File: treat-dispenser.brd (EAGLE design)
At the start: 31.8 x 47 mm, 36 parts, among them U1 MCP73831, U3 ATMEGA32U4, Y1 16MHz

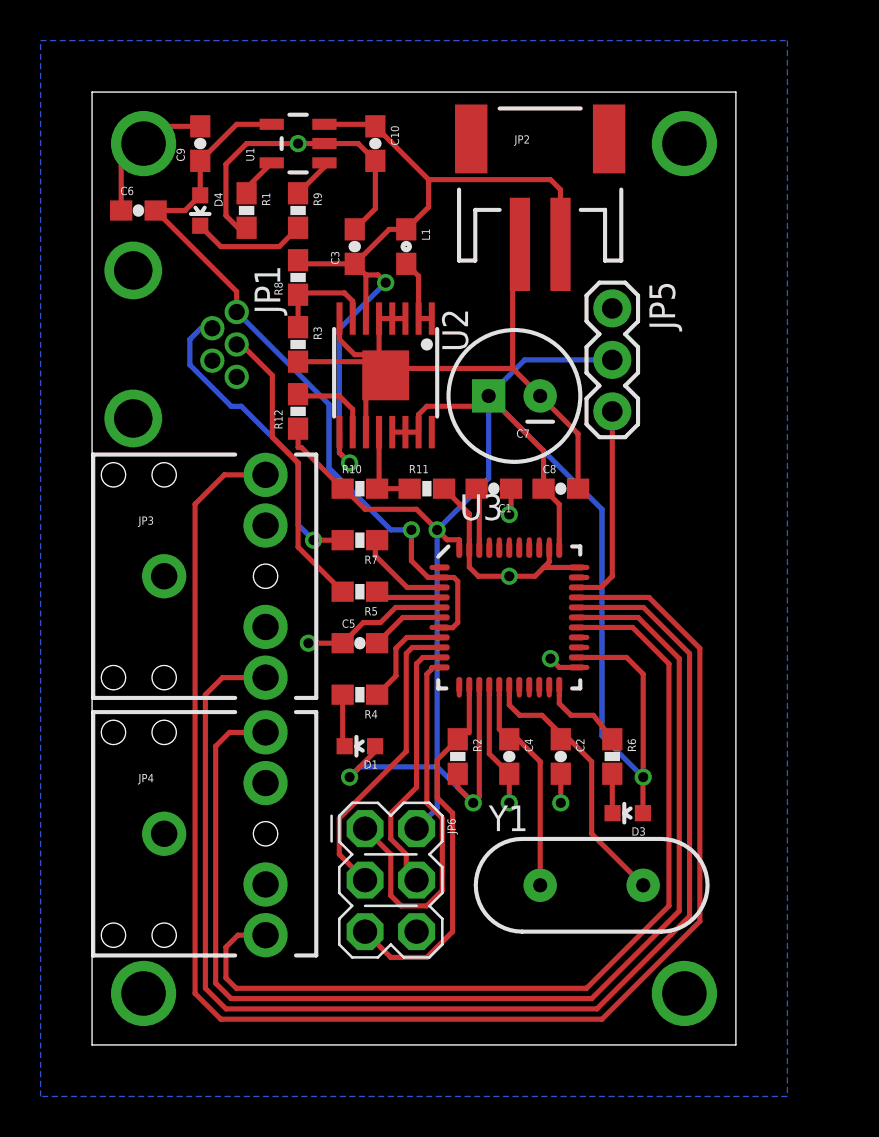
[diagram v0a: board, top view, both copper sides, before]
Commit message: fixed some routing issues, added part numbers
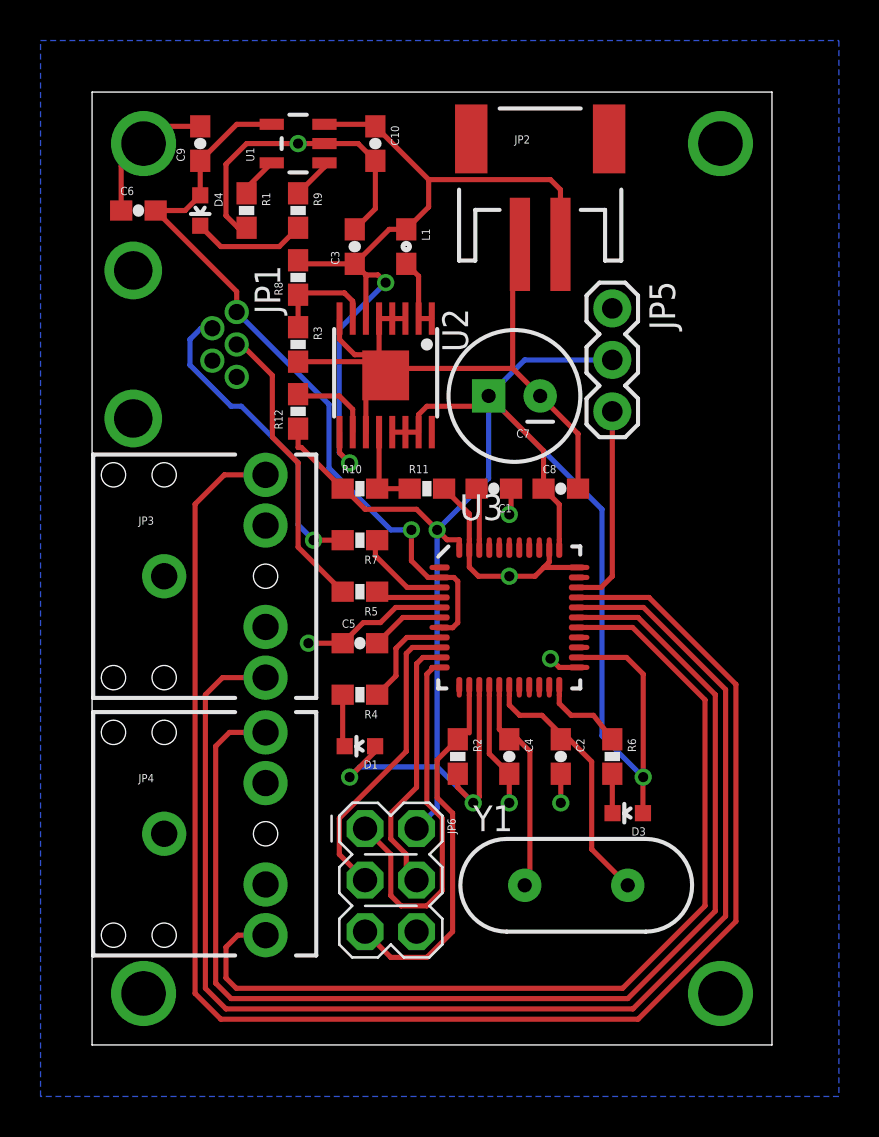
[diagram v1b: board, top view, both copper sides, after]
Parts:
- added FRAME1: FRAME-LETTER, SparkFun-Aesthetics:CREATIVE_COMMONS
- JP1: value USB-MB-H -> WM17115-ND
- U2: value (none) -> TPS61032
- moved Y1 0.76 mm to (23.9, 7.87)
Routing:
- net D9: track 62.9 -> 65.5 mm
- net D8: track 57.7 -> 60.2 mm
- net D10: track 75.7 -> 78.2 mm
- net D6: track 44.2 -> 46.7 mm
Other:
- board size 31.8 x 47 mm -> 33.5 x 47 mm
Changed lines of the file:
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@@
 <layer number="19" name="Unrouted" color="6" fill="1" visible="yes" active="yes"/>
 <layer number="20" name="Dimension" color="15" fill="1" visible="yes" active="yes"/>
-<layer number="21" name="tPlace" color="7" fill="1" visible="yes" active="yes"/>
-<layer number="22" name="bPlace" color="7" fill="1" visible="yes" active="yes"/>
+<layer number="21" name="tPlace" color="14" fill="1" visible="yes" active="yes"/>
+<layer number="22" name="bPlace" color="14" fill="1" visible="yes" active="yes"/>
 <layer number="23" name="tOrigins" color="15" fill="1" visible="yes" active="yes"/>
 <layer number="24" name="bOrigins" color="15" fill="1" visible="yes" active="yes"/>
@@
 <board>
 <plain>
-<wire x1="0" y1="0" x2="31.75" y2="0" width="0" layer="20"/>
-<wire x1="31.75" y1="0" x2="31.75" y2="46.99" width="0" layer="20"/>
-<wire x1="31.75" y1="46.99" x2="0" y2="46.99" width="0" layer="20"/>
+<wire x1="0" y1="0" x2="33.528" y2="0" width="0" layer="20"/>
+<wire x1="33.528" y1="0" x2="33.528" y2="46.99" width="0" layer="20"/>
+<wire x1="33.528" y1="46.99" x2="0" y2="46.99" width="0" layer="20"/>
 <wire x1="0" y1="46.99" x2="0" y2="0" width="0" layer="20"/>
 </plain>
@@
 <element name="D3" library="SparkFun" package="LED-0603" value="Green" x="26.416" y="11.43" rot="R90"/>
 <element name="U3" library="Testing" package="QFN-44-NOPAD_1:1-OUTFAKES" value="ATMEGA32U4" x="20.574" y="21.082"/>
-<element name="Y1" library="SparkFun" package="HC49US" value="16MHz" x="24.638" y="7.874"/>
+<element name="Y1" library="SparkFun" package="HC49US" value="16MHz" x="23.876" y="7.874"/>
 <element name="C2" library="SparkFun" package="0603-CAP" value="22pF" x="23.114" y="14.224" rot="R270"/>
 <element name="C4" library="SparkFun" package="0603-CAP" value="22pF" x="20.574" y="14.224" rot="R270"/>
@@
 <element name="R5" library="SparkFun" package="0603-RES" value="22" x="13.208" y="22.352" rot="R180"/>
 <element name="R7" library="SparkFun" package="0603-RES" value="22" x="13.208" y="24.892" rot="R180"/>
-<element name="JP1" library="SparkFun-Connectors" package="USB-MB-H" value="USB-MB-H" x="2.032" y="34.544"/>
+<element name="JP1" library="SparkFun-Connectors" package="USB-MB-H" value="WM17115-ND" x="2.032" y="34.544"/>
 <element name="C9" library="SparkFun" package="0603-CAP" value="4.7uF" x="5.334" y="44.45" rot="R90"/>
 <element name="C10" library="SparkFun" package="0603-CAP" value="4.7uF" x="13.97" y="44.45" rot="R270"/>
@@
 <element name="R1" library="SparkFun" package="0603-RES" value="10K" x="7.62" y="41.148" rot="R270"/>
 <element name="JP2" library="SparkFun" package="JST-2-SMD" value="LiPo" x="22.098" y="43.18"/>
-<element name="U2" library="tps6103x" package="TSSOP-16" value="" x="14.478" y="33.02" rot="R180"/>
+<element name="U2" library="tps6103x" package="TSSOP-16" value="TPS61032" x="14.478" y="33.02" rot="R180"/>
 <element name="R3" library="SparkFun" package="0603-RES" value="300K" x="10.16" y="34.544" rot="R270"/>
 <element name="R8" library="SparkFun" package="0603-RES" value="1.62M" x="10.16" y="37.846" rot="R90"/>
@@
 <element name="C7" library="SparkFun-Capacitors" package="CPOL-RADIAL-100UF-25V" value="220uF" x="20.828" y="32.004" rot="R180"/>
 <element name="C8" library="SparkFun" package="0603-CAP" value="10uF" x="23.114" y="27.432"/>
+<element name="FRAME1" library="SparkFun-Aesthetics" package="CREATIVE_COMMONS" value="FRAME-LETTER" x="19.05" y="49.53"/>
 </elements>
 <signals>
@@
 <contactref element="U2" pad="PAD"/>
 <via x="2.54" y="44.45" extent="1-16" drill="2.2"/>
-<via x="29.21" y="44.45" extent="1-16" drill="2.2"/>
+<via x="30.988" y="44.45" extent="1-16" drill="2.2"/>
 <via x="2.54" y="2.54" extent="1-16" drill="2.2"/>
-<via x="29.21" y="2.54" extent="1-16" drill="2.2"/>
+<via x="30.988" y="2.54" extent="1-16" drill="2.2"/>
 <polygon width="0.254" layer="16">
 <vertex x="-2.54" y="49.53"/>
-<vertex x="34.29" y="49.53"/>
-<vertex x="34.29" y="-2.54"/>
+<vertex x="36.83" y="49.53"/>
+<vertex x="36.83" y="-2.54"/>
 <vertex x="-2.54" y="-2.54"/>
 </polygon>
@@
 <wire x1="5.588" y1="17.272" x2="5.588" y2="2.794" width="0.254" layer="1"/>
 <wire x1="5.588" y1="2.794" x2="6.604" y2="1.778" width="0.254" layer="1"/>
-<wire x1="6.604" y1="1.778" x2="24.892" y2="1.778" width="0.254" layer="1"/>
-<wire x1="24.892" y1="1.778" x2="29.464" y2="6.35" width="0.254" layer="1"/>
-<wire x1="29.464" y1="6.35" x2="29.464" y2="19.304" width="0.254" layer="1"/>
+<wire x1="6.604" y1="1.778" x2="26.67" y2="1.778" width="0.254" layer="1"/>
+<wire x1="26.67" y1="1.778" x2="31.242" y2="6.35" width="0.254" layer="1"/>
+<wire x1="31.242" y1="6.35" x2="31.242" y2="17.526" width="0.254" layer="1"/>
 <wire x1="24.4035" y1="21.575" x2="27.193" y2="21.575" width="0.254" layer="1"/>
-<wire x1="27.193" y1="21.575" x2="29.464" y2="19.304" width="0.254" layer="1"/>
+<wire x1="27.193" y1="21.575" x2="31.242" y2="17.526" width="0.254" layer="1"/>
 </signal>
 <signal name="D8">
@@
 <contactref element="JP4" pad="RING"/>
 <wire x1="23.9105" y1="21.082" x2="26.924" y2="21.082" width="0.254" layer="1"/>
-<wire x1="26.924" y1="21.082" x2="28.956" y2="19.05" width="0.254" layer="1"/>
-<wire x1="28.956" y1="19.05" x2="28.956" y2="6.604" width="0.254" layer="1"/>
-<wire x1="28.956" y1="6.604" x2="24.638" y2="2.286" width="0.254" layer="1"/>
-<wire x1="24.638" y1="2.286" x2="6.858" y2="2.286" width="0.254" layer="1"/>
+<wire x1="26.924" y1="21.082" x2="30.734" y2="17.272" width="0.254" layer="1"/>
+<wire x1="30.734" y1="17.272" x2="30.734" y2="6.604" width="0.254" layer="1"/>
+<wire x1="30.734" y1="6.604" x2="26.416" y2="2.286" width="0.254" layer="1"/>
+<wire x1="26.416" y1="2.286" x2="6.858" y2="2.286" width="0.254" layer="1"/>
 <wire x1="6.858" y1="2.286" x2="6.096" y2="3.048" width="0.254" layer="1"/>
 <wire x1="8.556" y1="15.414" x2="6.778" y2="15.414" width="0.254" layer="1"/>
@@
 <wire x1="6.604" y1="4.826" x2="6.604" y2="3.302" width="0.254" layer="1"/>
 <wire x1="6.604" y1="3.302" x2="7.112" y2="2.794" width="0.254" layer="1"/>
-<wire x1="7.112" y1="2.794" x2="24.384" y2="2.794" width="0.254" layer="1"/>
-<wire x1="24.384" y1="2.794" x2="28.448" y2="6.858" width="0.254" layer="1"/>
+<wire x1="7.112" y1="2.794" x2="26.162" y2="2.794" width="0.254" layer="1"/>
+<wire x1="26.162" y1="2.794" x2="30.226" y2="6.858" width="0.254" layer="1"/>
 <wire x1="24.4035" y1="20.589" x2="26.655" y2="20.589" width="0.254" layer="1"/>
-<wire x1="26.655" y1="20.589" x2="28.448" y2="18.796" width="0.254" layer="1"/>
-<wire x1="28.448" y1="18.796" x2="28.448" y2="6.858" width="0.254" layer="1"/>
+<wire x1="26.655" y1="20.589" x2="30.226" y2="17.018" width="0.254" layer="1"/>
+<wire x1="30.226" y1="17.018" x2="30.226" y2="6.858" width="0.254" layer="1"/>
 </signal>
 <signal name="D7">
@@
 <wire x1="5.08" y1="26.67" x2="5.08" y2="2.54" width="0.254" layer="1"/>
 <wire x1="5.08" y1="2.54" x2="6.35" y2="1.27" width="0.254" layer="1"/>
-<wire x1="6.35" y1="1.27" x2="25.146" y2="1.27" width="0.254" layer="1"/>
-<wire x1="25.146" y1="1.27" x2="29.972" y2="6.096" width="0.254" layer="1"/>
+<wire x1="6.35" y1="1.27" x2="26.924" y2="1.27" width="0.254" layer="1"/>
+<wire x1="26.924" y1="1.27" x2="31.75" y2="6.096" width="0.254" layer="1"/>
 <wire x1="24.4035" y1="22.068" x2="27.462" y2="22.068" width="0.254" layer="1"/>
-<wire x1="27.462" y1="22.068" x2="29.972" y2="19.558" width="0.254" layer="1"/>
-<wire x1="29.972" y1="19.558" x2="29.972" y2="6.096" width="0.254" layer="1"/>
+<wire x1="27.462" y1="22.068" x2="31.75" y2="17.78" width="0.254" layer="1"/>
+<wire x1="31.75" y1="17.78" x2="31.75" y2="6.096" width="0.254" layer="1"/>
 </signal>
 <signal name="N$1">
@@
 <contactref element="C4" pad="1"/>
 <wire x1="20.081" y1="17.2525" x2="20.081" y2="15.567" width="0.254" layer="1"/>
-<wire x1="22.098" y1="13.97" x2="22.098" y2="7.874" width="0.254" layer="1"/>
 <wire x1="20.081" y1="15.567" x2="20.574" y2="15.074" width="0.254" layer="1"/>
 <wire x1="20.574" y1="15.074" x2="20.994" y2="15.074" width="0.254" layer="1"/>
-<wire x1="20.994" y1="15.074" x2="22.098" y2="13.97" width="0.254" layer="1"/>
+<wire x1="20.994" y1="15.074" x2="21.59" y2="14.478" width="0.254" layer="1"/>
+<wire x1="21.59" y1="14.478" x2="21.59" y2="8.128" width="0.254" layer="1"/>
+<wire x1="21.59" y1="8.128" x2="21.336" y2="7.874" width="0.254" layer="1"/>
 </signal>
 <signal name="N$2">
@@
 <wire x1="20.574" y1="16.764" x2="21.082" y2="16.256" width="0.254" layer="1"/>
 <wire x1="21.082" y1="16.256" x2="22.186" y2="16.256" width="0.254" layer="1"/>
-<wire x1="24.638" y1="13.97" x2="24.638" y2="10.414" width="0.254" layer="1"/>
-<wire x1="24.638" y1="10.414" x2="27.178" y2="7.874" width="0.254" layer="1"/>
+<wire x1="24.638" y1="13.97" x2="24.638" y2="9.652" width="0.254" layer="1"/>
 <wire x1="23.114" y1="15.074" x2="23.114" y2="15.328" width="0.254" layer="1"/>
 <wire x1="23.114" y1="15.328" x2="22.186" y2="16.256" width="0.254" layer="1"/>
 <wire x1="23.114" y1="15.074" x2="23.534" y2="15.074" width="0.254" layer="1"/>
 <wire x1="23.534" y1="15.074" x2="24.638" y2="13.97" width="0.254" layer="1"/>
+<wire x1="24.638" y1="9.652" x2="26.416" y2="7.874" width="0.254" layer="1"/>
 </signal>
 <signal name="RXI">

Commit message: minor fixes and part changes, added status led
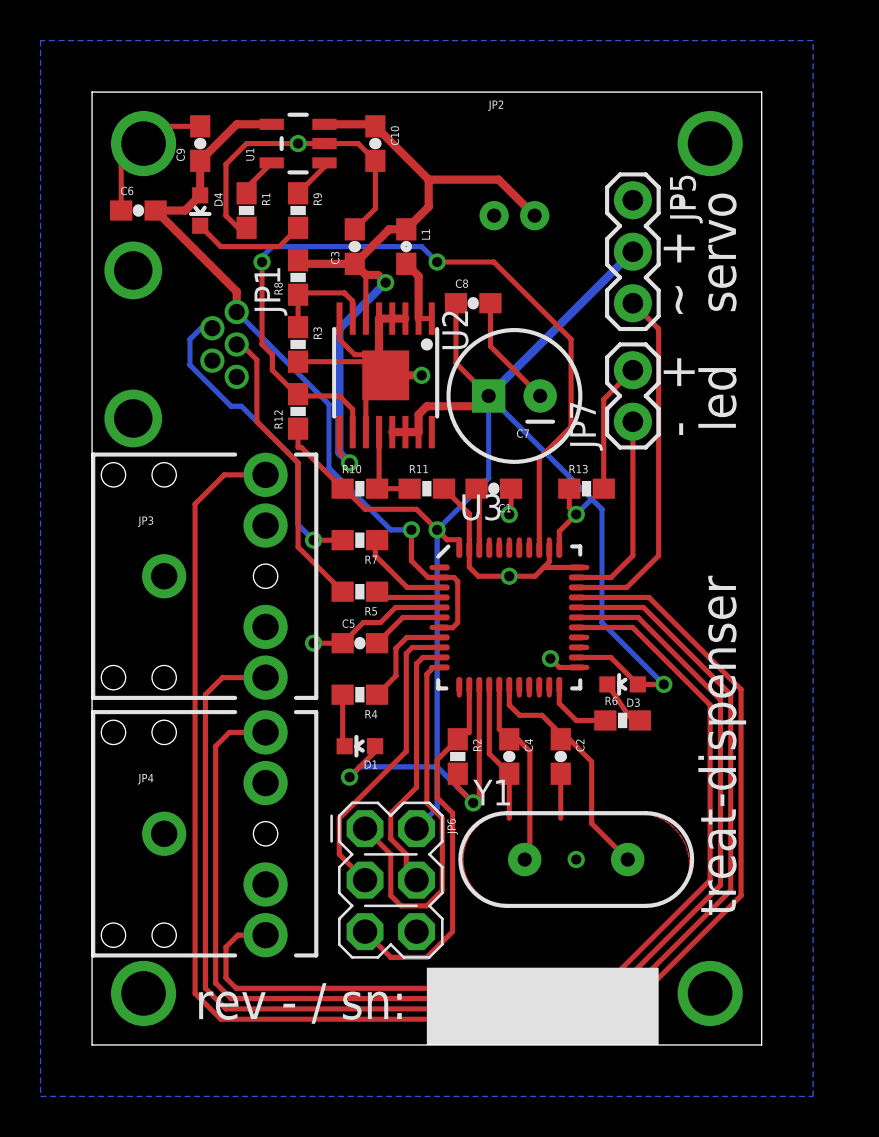
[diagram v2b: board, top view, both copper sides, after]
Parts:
- added JP7: (no value), SparkFun-Connectors:1X02
- added R13: 470, SparkFun:0603-RES
- JP2: value LiPo -> (none); device SparkFun:JST-2-SMD -> SparkFun-Connectors:JST-2-PTH-KIT
- JP3, JP4: value (none) -> SJ1-3523N
- moved C8 10.1 mm to (18.8, 36.6)
- moved D3 6.36 mm to (26.2, 17.8)
- moved JP5 5.43 mm to (26.7, 41.7)
- moved JP2 2.62 mm to (20.8, 40.9)
- moved R6 1.85 mm to (26.2, 16.0), turned to 0 degrees
- moved Y1 1.27 mm to (23.9, 9.14)
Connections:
- removed net ASD: R12.2, U2.10
- new net N$8: JP7.2, R13.2
- net A0: now also R12.2, U2.10
- net D13: now also JP7.1
- net VCC: now also R13.1
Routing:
- net A0: track 0.00 -> 39.6 mm, vias 0 -> 2
- net GND: track 86.2 -> 74.7 mm
- net D13: track 0.00 -> 9.32 mm
- net D5: track 9.61 -> 17.2 mm
- net N$8: track 0.00 -> 6.44 mm
- net VCC: track 103.1 -> 97.9 mm, vias 4 -> 5
- net ASD: track 4.13 -> 0.00 mm
- net V_BATT: track 40.6 -> 37.2 mm
- net N$2: track 12.7 -> 11.4 mm
- net N$1: track 10.4 -> 9.08 mm
- net D8: track 60.2 -> 59.4 mm
- net TXLED: track 3.84 -> 3.03 mm
- net N$7: track 1.95 -> 2.48 mm
- added copper zone on layer 1, net GND
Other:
- board size 33.5 x 47 mm -> 33 x 47 mm
- board text added: "+"
- board text added: "-"
- board text added: "led"
- board text added: "rev - / sn:"
- board text added: "servo"
- board text added: "treat-dispenser"
- board text added: "~"

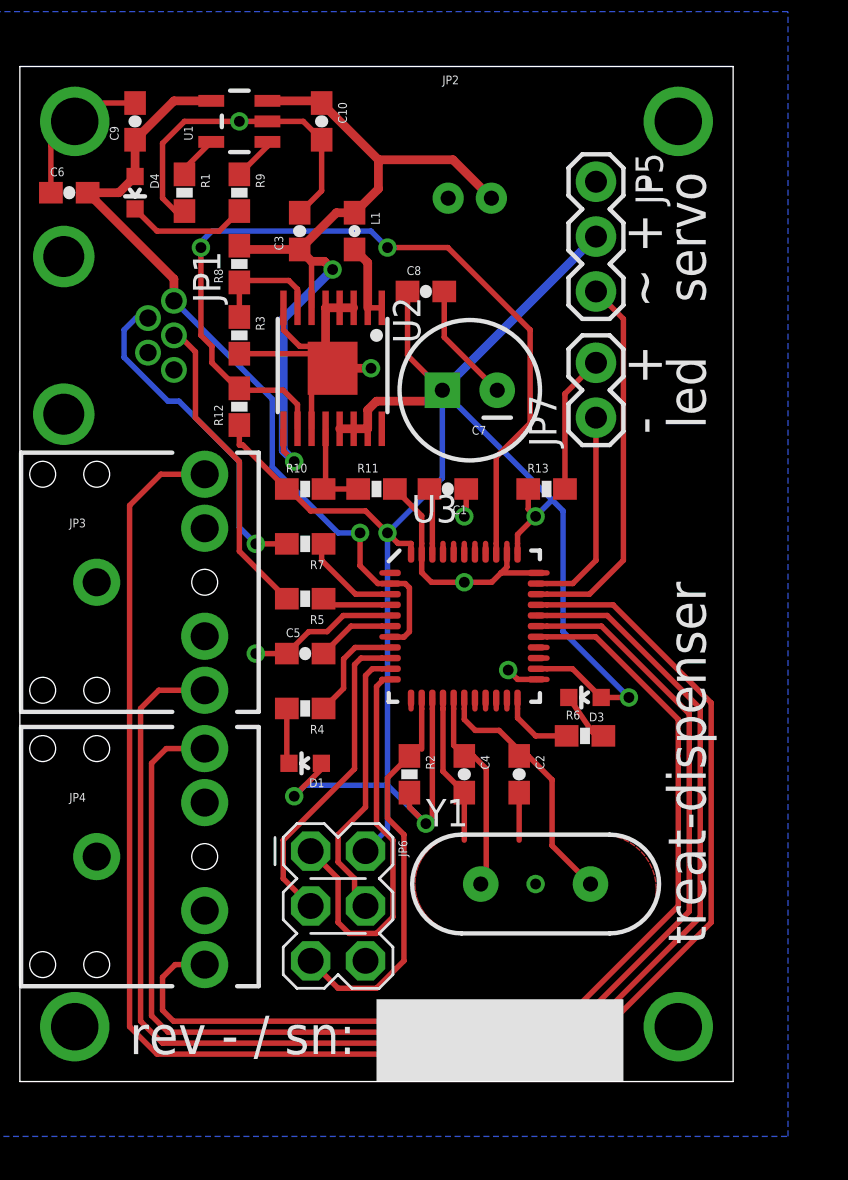
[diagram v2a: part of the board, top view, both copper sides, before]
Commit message: added optional sensor, cleaned up for mfg
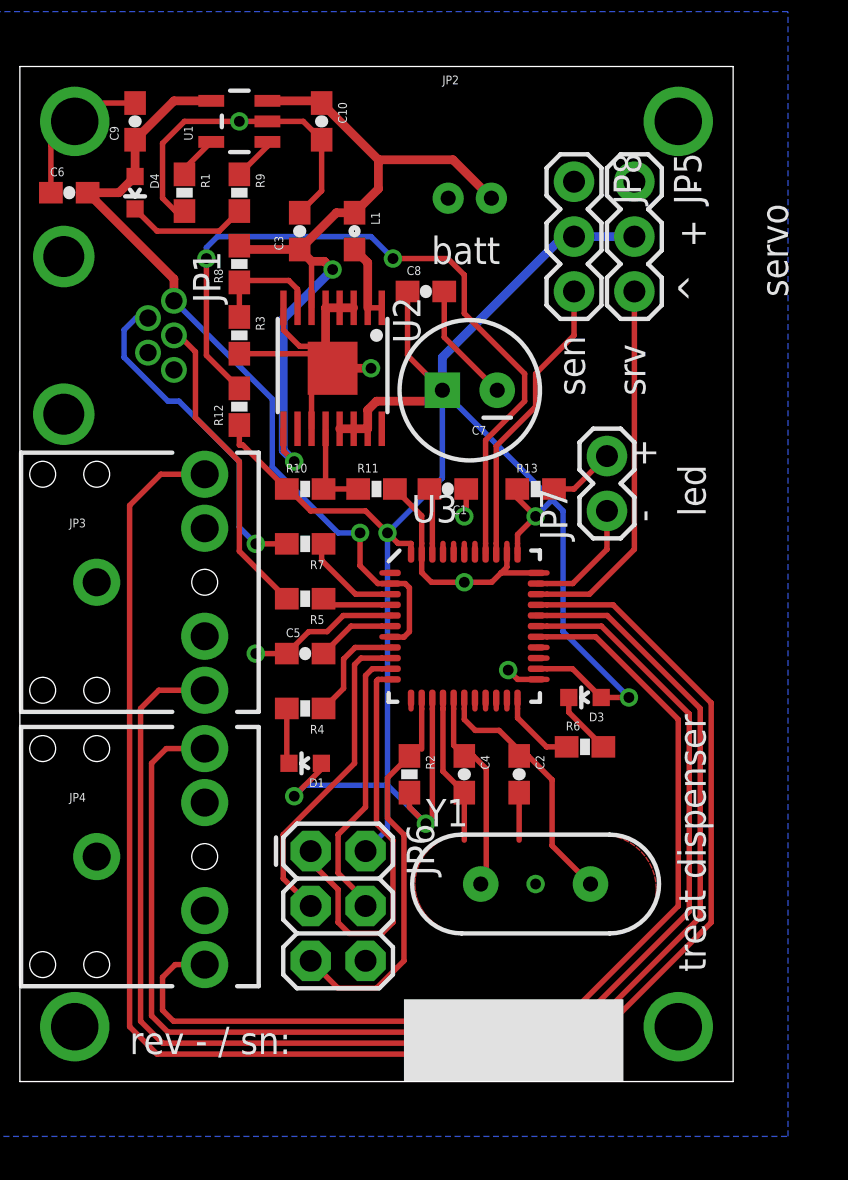
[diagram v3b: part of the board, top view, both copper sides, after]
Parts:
- added JP8: (no value), SparkFun-Connectors:1X03
- JP6: value (none) -> FEMALE 2x3; device SparkFun-Connectors:2X3_POGO -> SparkFun-Connectors:2X3
- moved JP7 4.35 mm to (27.2, 26.4)
- moved JP5 1.78 mm to (28.4, 41.7)
- moved R13 0.51 mm to (23.9, 27.4)
- moved R6 0.51 mm to (26.2, 15.5)
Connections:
- net A0: now also JP8.3; no longer R12.2, U2.10
- net A1: now also R12.2, U2.10
- net GND: now also JP6.6, JP8.1; no longer JP6.P$6
- net MISO: now also JP6.1; no longer JP6.P$1
- net MOSI: now also JP6.4; no longer JP6.P$4
- net RESET: now also JP6.5; no longer JP6.P$5
- net SCK: now also JP6.3; no longer JP6.P$3
- net VCC: now also JP6.2, JP8.2; no longer JP6.P$2
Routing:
- net A1: track 0.00 -> 34.4 mm, vias 0 -> 2
- net A0: track 39.6 -> 13.2 mm, vias 2 -> 0
- net D13: track 9.32 -> 5.21 mm
- net N$8: track 6.44 -> 3.08 mm
- net VCC: track 97.9 -> 100.8 mm
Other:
- board text added: "^"
- board text added: "batt"
- board text added: "sen"
- board text added: "srv"
- board text added: "treat dispenser"
- board text removed: "treat-dispenser"
- board text removed: "~"
